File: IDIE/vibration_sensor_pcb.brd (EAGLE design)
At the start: 61.3 x 43.4 mm, 3 parts, among them IC1 LORA-E5, IC2 STM32L071KBT6

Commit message: add new design with other modules
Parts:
- added ANT1: ANTENNA, SamacSys_Parts:ANTENNA
- added IC3: FXLS8974CFR3, SamacSys_Parts:FXLS8974CFR3
- added IC4: FXLS8971CFR1, SamacSys_Parts:FXLS8971CFR1
- moved H1 53.2 mm to (58.0, 21.7)
- moved IC2 53.2 mm to (30.6, 6.07)
- moved IC1 49.6 mm to (24.9, 34.7)
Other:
- outline, holes or cut-outs redrawn

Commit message: UPLOADING todo el diseño nuevo de pcb con conexiones de spi e i2c
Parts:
- added C1, C2: DNP, rcl:C0603
- added C3: 4.7uF, rcl:C0603
- added C4, C5, C7: 0.1uF, rcl:C0603
- added C6: 1uF, rcl:C0603
- added JMP1, JMP2, JMP3: 0R-JUMPA, jump-0r-smd:A0R-JMP
- added Q1: SI2305B-TP, SamacSys_Parts:SOT95P237X125-3N
- added R1: 0, rcl:R0603
- added R2, R5, R6: 100k, rcl:R0603
- added R3, R4: 22, rcl:R0603
- added R7: DNP, rcl:R0603
- added T1: (no value), transistor-neu-to92:SC59-BEC
- added TP1, TP2, TP3, TP4, TP5: PTR1TP11R, testpad:TP11R
- moved ANT1 0.44 mm to (40.7, 40.7)
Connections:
- new net +3V3: C3.1, C4.1, C6.1, C7.1, IC1.1, IC2.1, IC2.17, IC2.5, IC3.1, IC4.1, JMP3.3, R2.2, R5.2, R6.2
- new net ANT: ANT1.1, C2.1, R1.2
- new net BOOT: IC1.24, TP3.TP
- new net E5_RST: C5.1, IC1.17, R2.1, T1.C
- new net GND: C1.2, C2.2, C3.2, C4.2, C5.2, C6.2, C7.2, H1.2, IC1.14, IC1.16, IC1.2, IC1.22, IC2.16, IC2.32, IC3.10, IC3.2, IC4.10, IC4.2, JMP3.1, R7.1, T1.E
- new net I2C_SCL: IC2.19
- new net I2C_SDA: IC2.20
- new net INT1: IC3.8, IC4.8, R6.1
- new net INT2: IC3.6, IC4.6, R5.1
- new net MCU_RXD: IC2.9, R3.2
- new net MCU_SWCLK: IC2.24
- new net MCU_SWDIO: IC2.23
- new net MCU_TXD: IC2.8, R4.2
- new net MD_RST: T1.B
- new net N$1: IC3.9, IC4.9, JMP3.2
- new net N$3: IC1.10, R3.1, TP5.TP
- new net N$4: IC1.9, R4.1, TP4.TP
- new net PA15: IC2.25
- new net PA8: IC2.18
- new net PB3: IC2.26
- new net PB4: IC2.27
- new net PB5: IC2.28
- new net PB6: IC2.29
- new net PB7: IC2.30
- new net RF_IO: C1.1, IC1.15, R1.1
- new net SCL: JMP2.3
- new net SCL/SCLK: IC3.5, IC4.5, JMP2.2
- new net SDA: JMP1.3
- new net SDA/MOSI: IC3.4, IC4.4, JMP1.2
- new net SPI_CS: IC2.10, IC3.7, IC4.7
- new net SPI_MISO: IC2.12, IC3.3, IC4.3, R7.2
- new net SPI_MOSI: IC2.13, JMP1.1
- new net SPI_SCK: IC2.11
- new net SPI_SCLK: JMP2.1
- new net SWCLK: IC1.4, TP1.TP
- new net SWDIO: IC1.3, TP2.TP

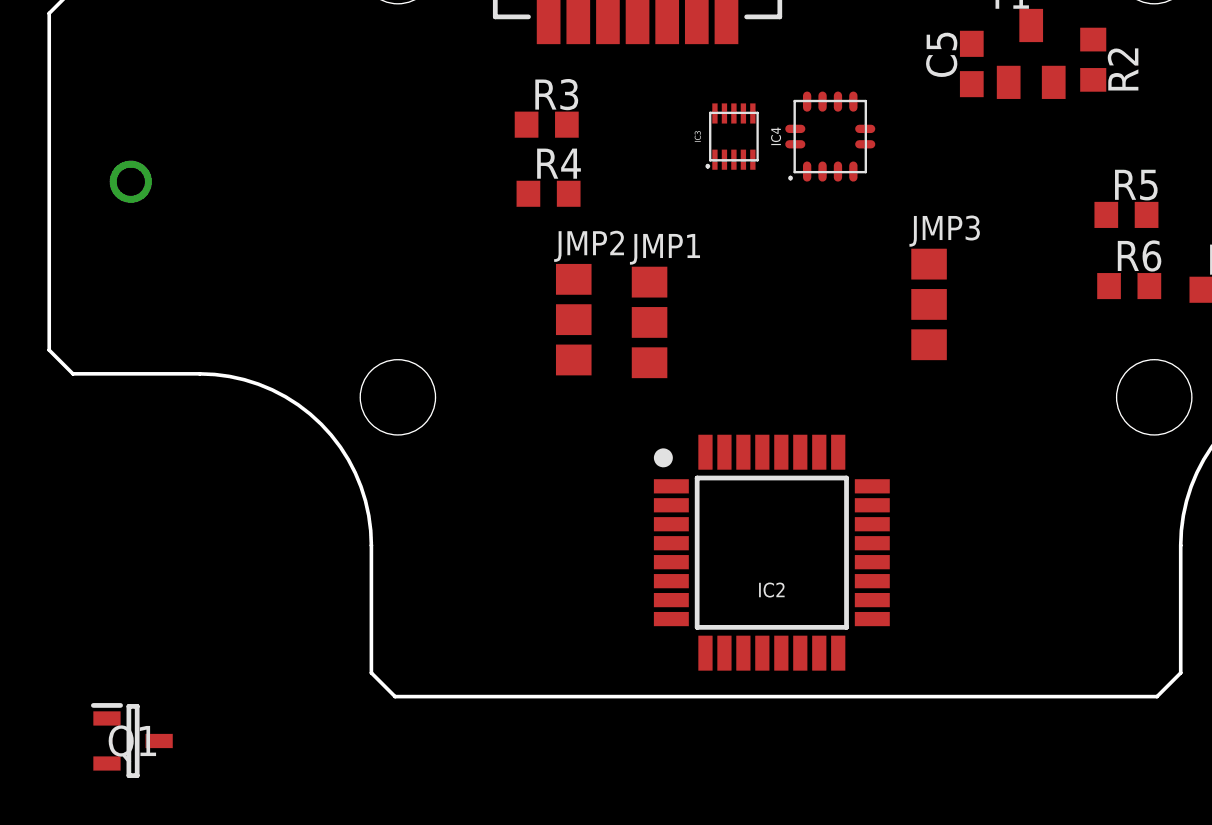
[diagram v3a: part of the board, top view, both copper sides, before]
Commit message: ADD crista sensor hall
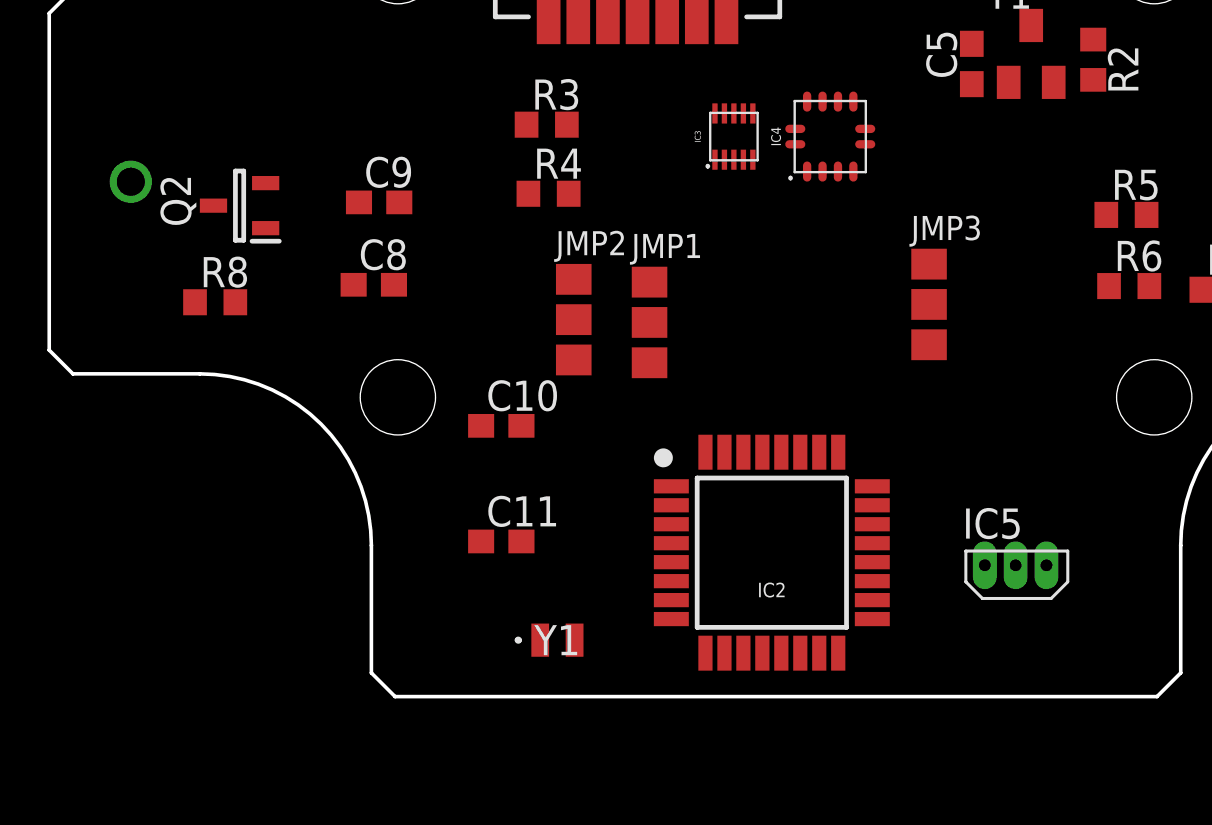
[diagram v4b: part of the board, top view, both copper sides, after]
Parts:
- removed Q1: SI2305B-TP, SamacSys_Parts:SOT95P237X125-3N
- added C10, C11: 12.5uF, rcl:C0603
- added C8: 1uF, rcl:C0603
- added C9: 0.1uF, rcl:C0603
- added IC5: DRV5032FBLPGM5HZ, transistor:DRV5032FBLPGM
- added Q2: SI2305B-TP, SamacSys_Parts:SOT95P237X125-3N
- added R8: 100k, rcl:R0603
- added Y1: ABS06-32.768KHZ-9-1-T, SamacSys_Parts:ABS06
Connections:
- new net N$2: H1.1, Q2.3
- new net N$6: Q2.1, R8.2
- new net N$7: C11.1, IC2.2, Y1.2
- new net N$8: C10.1, IC2.3, Y1.1
- new net SEND_OUT: IC5.2
- net +3V3: now also C8.1, C9.1, IC5.1, Q2.2
- net GND: now also C10.2, C11.2, C8.2, C9.2, IC5.3, R8.1

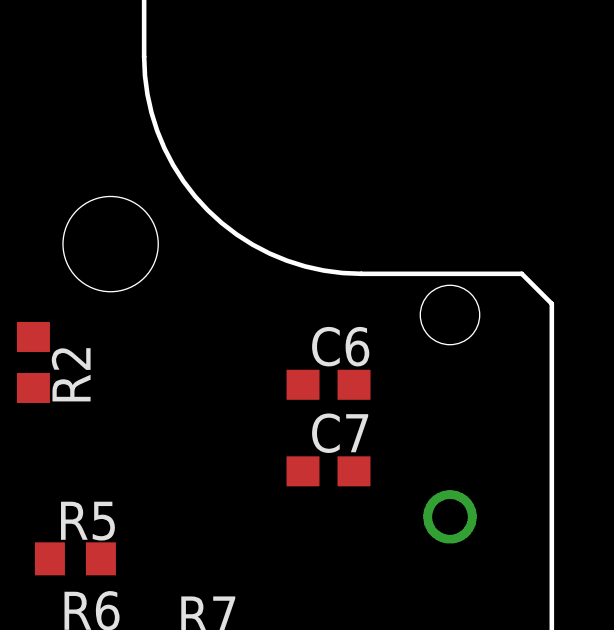
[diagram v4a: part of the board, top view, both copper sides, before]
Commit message: UPDATE se agregan y conectan componentes de pcb, mosfet, jumpers...
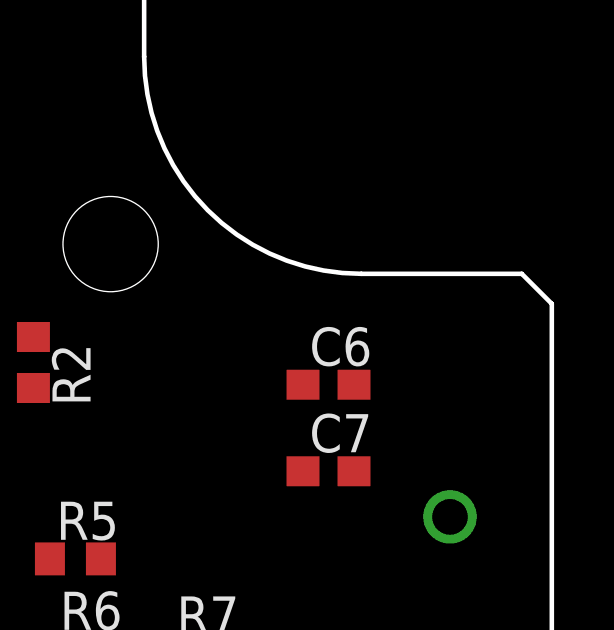
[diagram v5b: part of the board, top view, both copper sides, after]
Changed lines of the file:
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@@
 <wire x1="3.51798125" y1="21.717" x2="6.226" y2="16.634" width="0" layer="19" extent="1-1"/>
 <wire x1="33.3562" y1="1.8326" x2="27.7562" y2="10.3086" width="0" layer="19" extent="1-1"/>
-<wire x1="42.139" y1="5.54" x2="48.672" y2="17.161" width="0" layer="19" extent="1-1"/>
+<wire x1="42.139" y1="5.54" x2="33.3562" y2="1.8326" width="0" layer="19" extent="1-1"/>
 </signal>
 <signal name="+3V3">

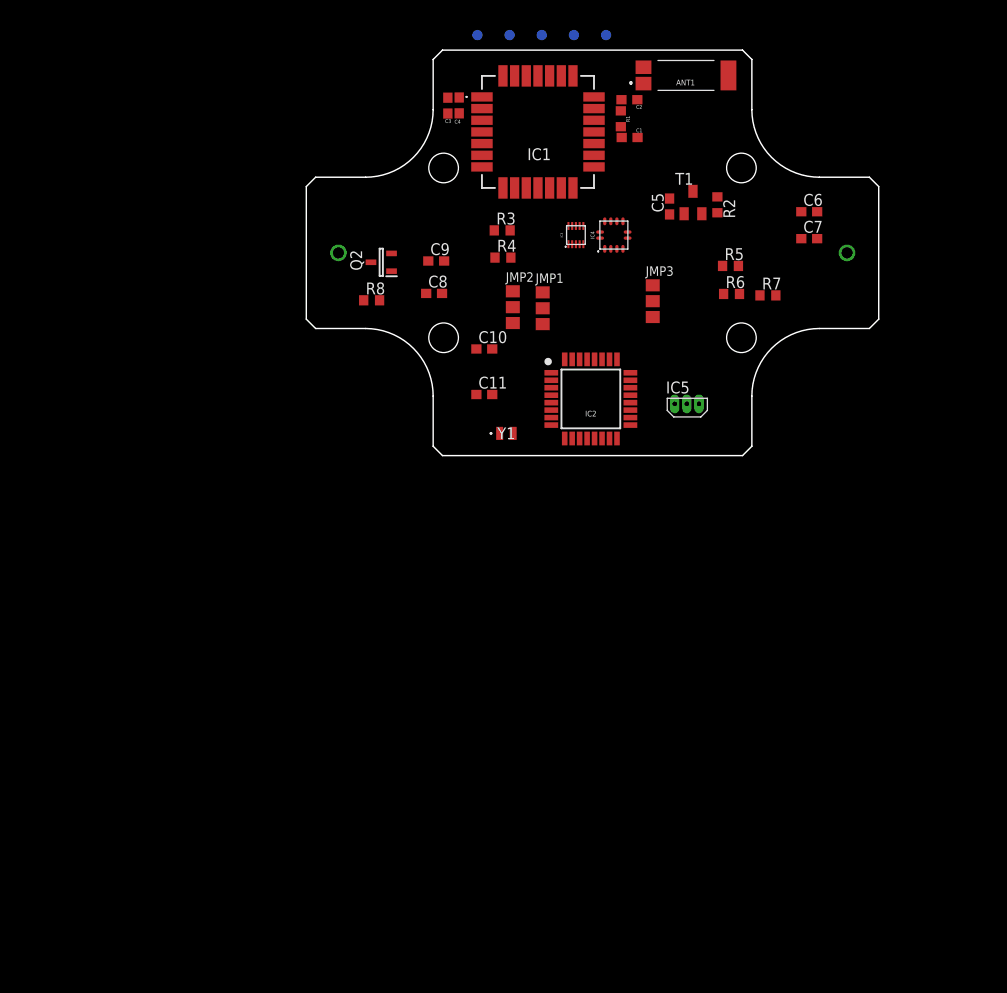
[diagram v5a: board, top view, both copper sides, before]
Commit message: UPDATE nueva hoja con usb y diversas conecciones antes de ruteo
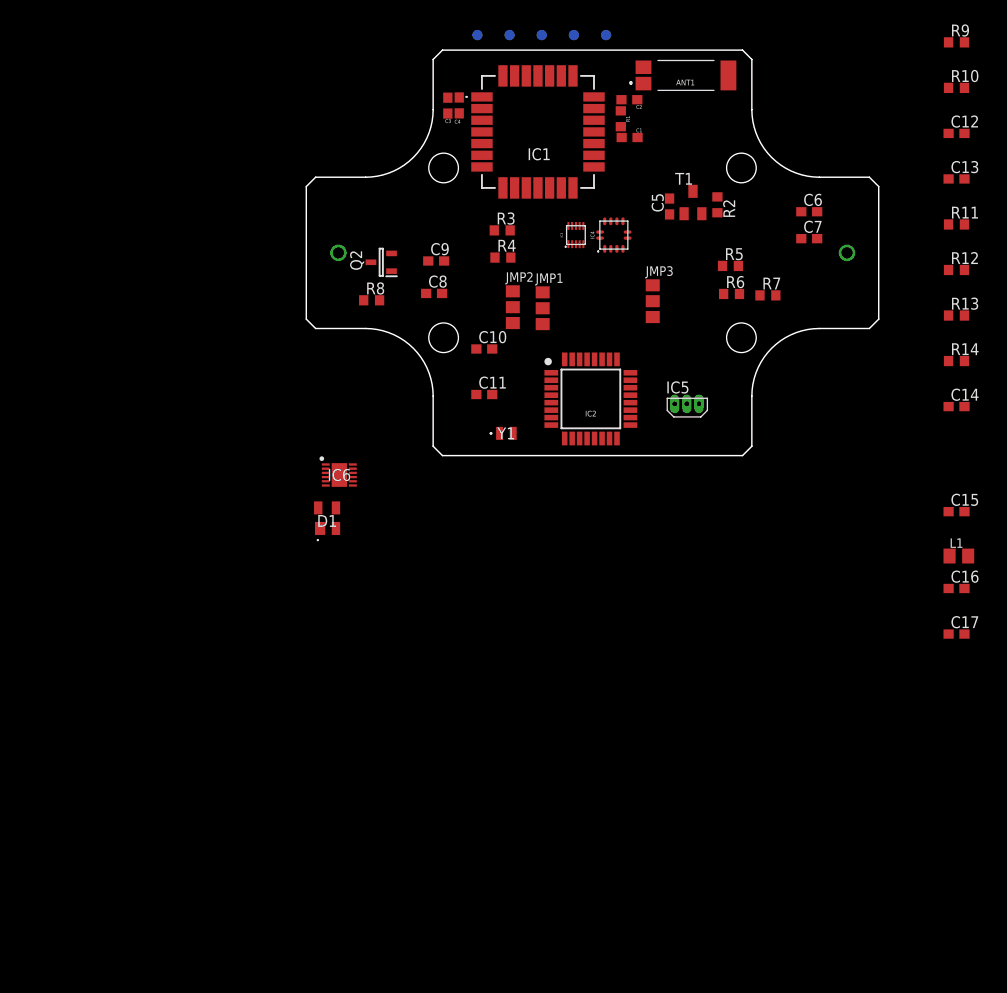
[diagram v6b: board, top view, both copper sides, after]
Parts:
- added C12, C13, C15, C16, C17: 47uF, rcl:C0603
- added C14: 0.1uF, rcl:C0603
- added D1: SP0503BAHTG, SamacSys_Parts:SP0503BAHTG
- added IC6: FT234XD-T, SamacSys_Parts:SON45P300X300X80-13N
- added L1: (no value), rcl:C0805K
- added R10, R9: 27, rcl:R0603
- added R11, R12, R13, R14: 22, rcl:R0603
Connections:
- new net N$10: IC6.12, R9.2
- new net N$11: IC6.1, R10.2
- new net N$12: IC6.7, R11.1
- new net N$13: IC6.10, R12.1
- new net N$14: IC6.8, R13.1
- new net N$16: IC6.11, R14.1
- new net N$17: R11.2
- new net N$18: R12.2
- new net N$19: R13.2
- new net N$20: R14.2
- new net N$9: C14.1, IC6.2, IC6.3, IC6.9
- new net USB_N: C13.1, D1.3, R10.1
- new net USB_P: C12.1, D1.2, R9.1
- new net VBUS: C15.1, D1.4, L1.1
- new net VCC: C16.1, C17.1, IC6.4, L1.2
- net GND: now also C12.2, C13.2, C14.2, C15.2, C16.2, C17.2, D1.1, IC6.13, IC6.5

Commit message: UPDATE casi terminacion del diseño, cambiar efecto hall y conectar ruteo
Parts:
- added C18: CLY6D-FKC-CK1N1D1BB7D3D3, SamacSys_Parts:PLCC6
- added J1: 217182-0001, SamacSys_Parts:2171820001
- added R15, R16: 27, rcl:R0603
- added R17, R18, R19: 22, rcl:R0603
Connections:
- removed net N$17: R11.2
- removed net N$18: R12.2
- removed net N$19: R13.2
- removed net N$20: R14.2
- removed net PA8: IC2.18
- removed net PB3: IC2.26
- removed net PB4: IC2.27
- removed net PB6: IC2.29
- removed net PB7: IC2.30
- new net LED_B: IC2.14, R17.2
- new net LED_G: IC2.15, R18.2
- new net LED_R: IC2.18, R19.2
- new net N$15: C18.6, R17.1
- new net N$21: J1.B5, R15.2
- new net N$22: J1.A5, R16.2
- new net N$23: C18.5, R18.1
- new net N$24: C18.4, R19.1
- new net PA0: IC2.6
- new net PA11: IC2.21
- new net PA12: IC2.22
- new net U1_CTS: IC2.27, R13.2
- new net U1_RTS: IC2.26, R14.2
- new net U1_RXD: IC2.30, R11.2
- new net U1_TXD: IC2.29, R12.2
- net GND: now also C18.1, C18.2, C18.3, J1.A1, J1.A12, J1.B1, J1.B12, J1.MH2, J1.MH3, J1.MH5, J1.MH6, R15.1, R16.1
- net SEND_OUT: now also IC2.7
- net USB_N: now also J1.A7, J1.B7
- net USB_P: now also J1.A6, J1.B6
- net VBUS: now also J1.A4, J1.A9, J1.B4, J1.B9

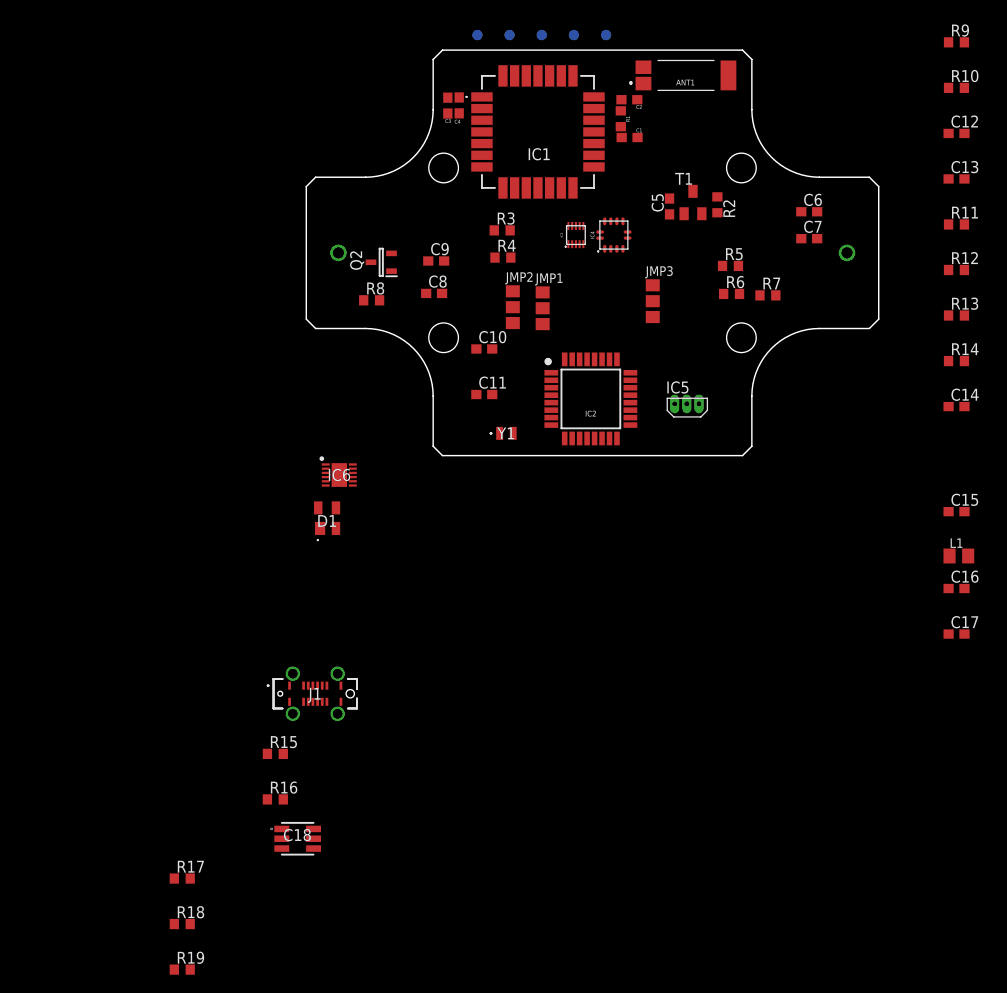
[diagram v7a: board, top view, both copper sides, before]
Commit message: UPDATE orden de pcb y reglas de diseño
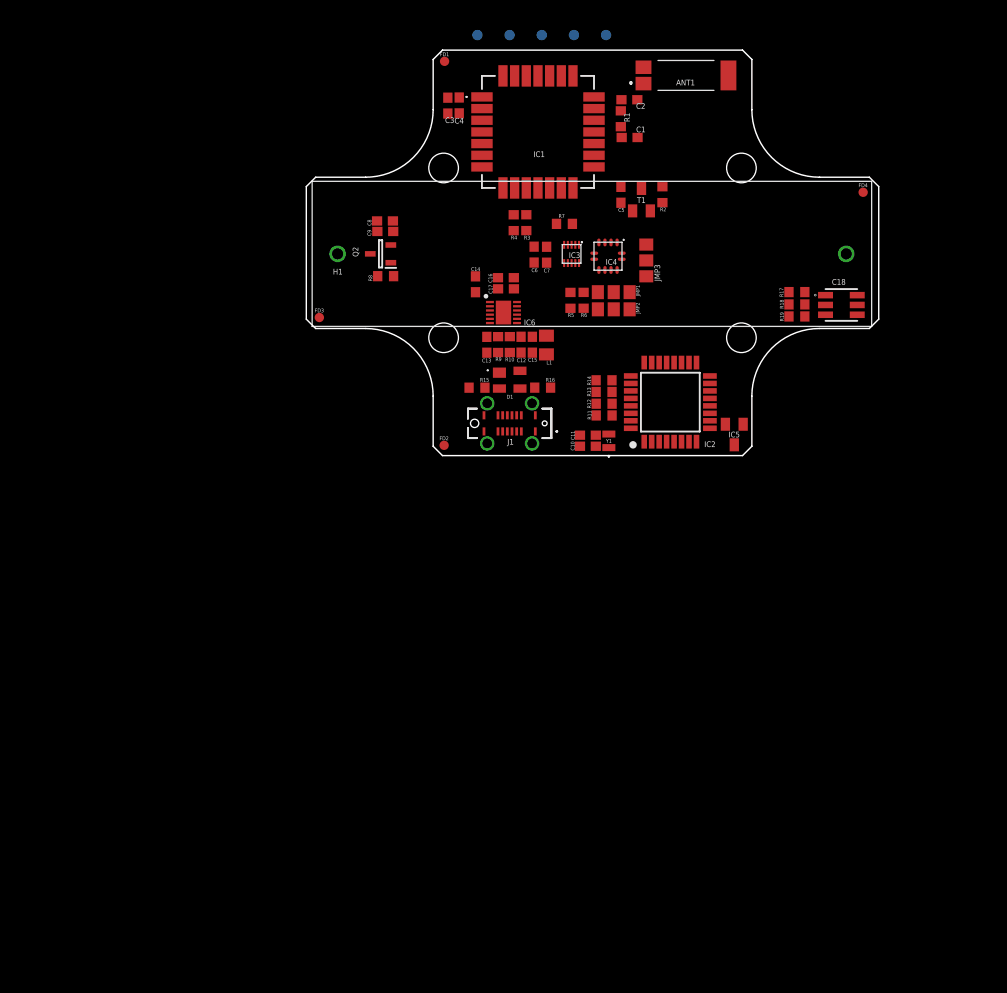
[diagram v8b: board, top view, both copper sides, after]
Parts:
- added FD1, FD2, FD3, FD4: TPTP10R, testpad:TP10R
- IC5: value DRV5032FBLPGM5HZ -> DRV5032FBLPGM; device transistor:DRV5032FBLPGM -> transistor:SOT23
- moved R19 96.1 mm to (52.6, 14.9)
- moved R18 93.5 mm to (52.6, 16.2)
- moved R17 91.0 mm to (52.6, 17.5)
- moved C18 81.6 mm to (57.4, 16.1)
- moved C17 60.8 mm to (21.5, 17.9)
- moved R9 58.8 mm to (20.6, 11.9), turned to 90 degrees
- moved C16 58.6 mm to (21.5, 19.1)
- moved R10 55.2 mm to (21.9, 11.9), turned to 90 degrees
- moved H1 54.6 mm to (3.43, 21.6), flipped to the top
- moved C13 53.4 mm to (19.4, 11.9), turned to 270 degrees
- moved C14 53.2 mm to (18.2, 18.4), turned to 270 degrees
- moved R16 52.6 mm to (25.4, 7.28), turned to 180 degrees
- moved C12 51.8 mm to (23.1, 11.9), turned to 270 degrees
- moved L1 49.6 mm to (25.8, 11.8), turned to 90 degrees
- moved C15 48.8 mm to (24.3, 11.9), turned to 90 degrees
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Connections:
- net N$10 renamed USBDP
- net N$11 renamed USBDM
- net N$12 renamed R11
- net N$13 renamed R12
- net N$14 renamed R13
- net N$15 renamed R17
- net N$16 renamed R14
- net N$2 renamed IN_MOSFET
- net N$21 renamed B5
- net N$22 renamed A5
- net N$23 renamed R18
- net N$24 renamed R19
- net N$3 renamed LORA_RXD
- net N$4 renamed LORA_TXD
- net N$7 renamed OSC32_IN
- net N$8 renamed OSC32_OUT
- net RF_IO renamed OUT_ANT
- removed net SPI_SCK: IC2.11
- net SPI_SCLK: now also IC2.11
